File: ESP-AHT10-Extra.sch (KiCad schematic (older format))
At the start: 27 parts, among them J1 USB, SW1 RESET, SW2 PROG, U1 CH330N, U2 HT7233, U3 ESP-12, U4 AHT10, U5 USBLC6-2SC6, U6 VEML7700

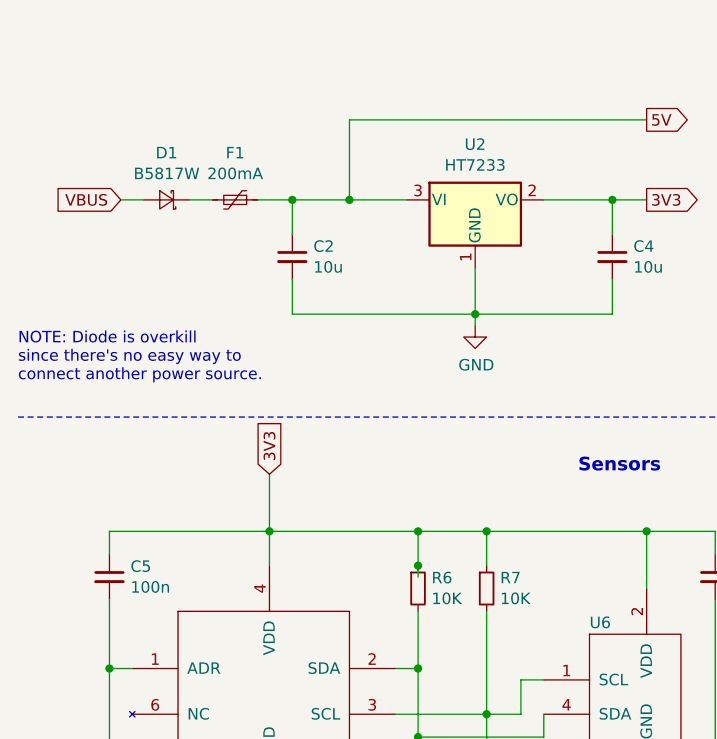
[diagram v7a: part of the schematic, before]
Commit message: a few trace tweaks
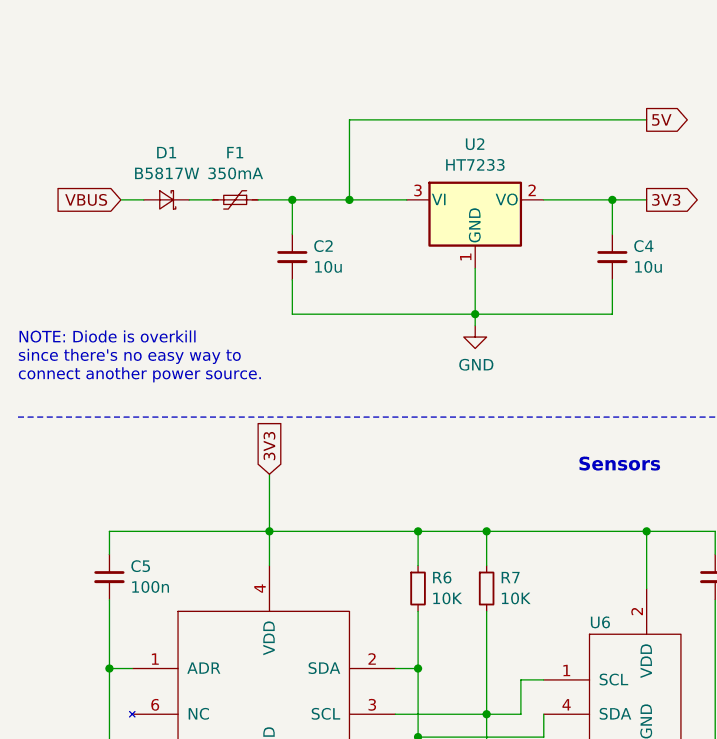
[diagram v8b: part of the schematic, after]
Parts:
- F1: value 200mA -> 350mA
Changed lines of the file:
@@
 P 1550 1350
 F 0 "F1" V 1345 1350 50  0000 C CNN
-F 1 "200mA" V 1436 1350 50  0000 C CNN
+F 1 "350mA" V 1436 1350 50  0000 C CNN
 F 2 "Fuse:Fuse_0805_2012Metric" H 1600 1150 50  0001 L CNN
 F 3 "~" H 1550 1350 50  0001 C CNN
@@
 Wire Wire Line
 	2650 2800 3350 2800
-Wire Wire Line
-	2350 3000 2350 2950
 Connection ~ 2350 2800
 Wire Wire Line
 	2350 2800 2650 2800
-Connection ~ 2350 2950
 Wire Wire Line
 	2350 2950 2350 2800
